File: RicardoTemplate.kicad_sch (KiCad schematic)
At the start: 38 parts, among them J1 RBUS, U1 ESP32-S3, Y1 R940000171

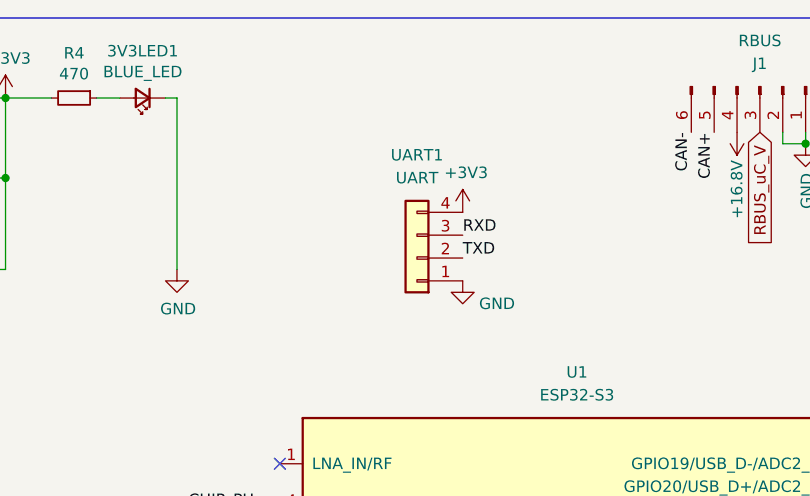
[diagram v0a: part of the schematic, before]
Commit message: Changed UART connector
Now with 1000% more nanofit!
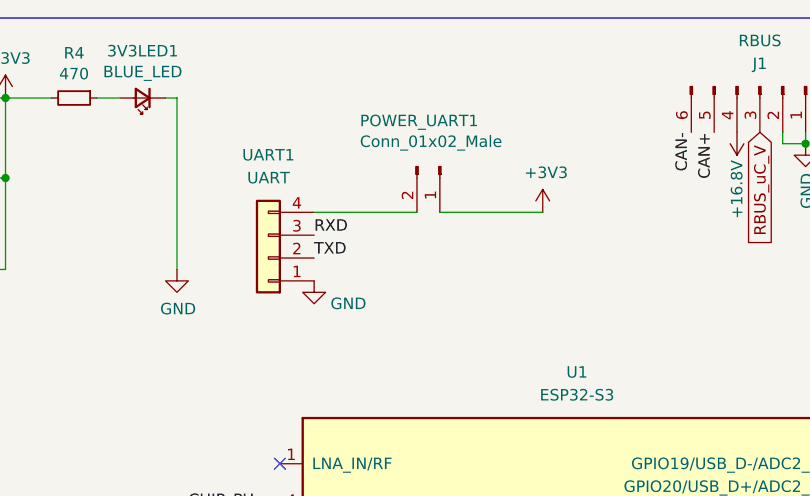
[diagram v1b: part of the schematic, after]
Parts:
- added POWER_UART1: Conn_01x02_Male, Connector_PinHeader_2.54mm:PinHeader_1x02_P2.54mm_Vertical, symbol Connector:Conn_01x02_Male
- UART1: footprint Connector_Molex:Molex_Mini-Fit_Jr_5566-04A_2x02_P4.20mm_Vertical -> Connector_Molex:Molex_Nano-Fit_105309-xx04_1x04_P2.50mm_Vertical
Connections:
- net +3V3: now also POWER_UART1.1 (Pin_1); no longer UART1.4 (Pin_4)
- new net: POWER_UART1.2 (Pin_2), UART1.4 (Pin_4)
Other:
- moved on the sheet: UART1
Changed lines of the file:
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@@
 	(wire
 		(pts
+			(xy 85.09 34.29) (xy 73.66 34.29)
+		)
+		(stroke
+			(width 0)
+			(type default)
+		)
+	)
+	(wire
+		(pts
 			(xy 156.21 127) (xy 156.21 128.27)
 		)
@@
 	(wire
 		(pts
+			(xy 99.06 34.29) (xy 87.63 34.29)
+		)
+		(stroke
+			(width 0)
+			(type default)
+		)
+	)
+	(wire
+		(pts
 			(xy 27.94 30.48) (xy 30.48 30.48)
 		)
@@
 	)
 	(label "RXD"
-		(at 90.17 36.83 0)
+		(at 73.66 36.83 0)
 		(fields_autoplaced yes)
 		(effects
@@
 	)
 	(label "TXD"
-		(at 90.17 39.37 0)
+		(at 73.66 39.37 0)
 		(fields_autoplaced yes)
 		(effects
@@
 	(symbol
 		(lib_id "power:+3.3V")
-		(at 90.17 34.29 0)
+		(at 99.06 34.29 0)
 		(unit 1)
 		(exclude_from_sim no)
@@
 		(dnp no)
 		(property "Reference" "#PWR052"
-			(at 90.17 38.1 0)
+			(at 99.06 38.1 0)
 			(effects
 				(font
@@
 		)
 		(property "Value" "+3V3"
-			(at 90.551 29.8958 0)
+			(at 99.441 29.8958 0)
 			(effects
 				(font
@@
 		)
 		(property "Footprint" ""
-			(at 90.17 34.29 0)
+			(at 99.06 34.29 0)
 			(effects
 				(font
@@
 		)
 		(property "Datasheet" ""
-			(at 90.17 34.29 0)
+			(at 99.06 34.29 0)
 			(effects
 				(font
@@
 		)
 		(property "Description" ""
-			(at 90.17 34.29 0)
+			(at 99.06 34.29 0)
 			(effects
 				(font
@@
 	(symbol
 		(lib_id "Connector_Generic:Conn_01x04")
-		(at 85.09 39.37 180)
+		(at 68.58 39.37 180)
 		(unit 1)
 		(exclude_from_sim no)
@@
 		(fields_autoplaced yes)
 		(property "Reference" "UART1"
-			(at 85.09 27.94 0)
+			(at 68.58 27.94 0)
 			(effects
 				(font
@@
 		)
 		(property "Value" "UART"
-			(at 85.09 30.48 0)
+			(at 68.58 30.48 0)
 			(effects
 				(font
@@
 			)
 		)
-		(property "Footprint" "Connector_Molex:Molex_Mini-Fit_Jr_5566-04A_2x02_P4.20mm_Vertical"
-			(at 85.09 39.37 0)
+		(property "Footprint" "Connector_Molex:Molex_Nano-Fit_105309-xx04_1x04_P2.50mm_Vertical"
+			(at 68.58 39.37 0)
 			(effects
 				(font
@@
 		)
 		(property "Datasheet" "~"
-			(at 85.09 39.37 0)
+			(at 68.58 39.37 0)
 			(effects
 				(font
@@
 		)
 		(property "Description" "Generic connector, single row, 01x04, script generated (kicad-library-utils/schlib/autogen/connector/)"
-			(at 85.09 39.37 0)
+			(at 68.58 39.37 0)
 			(effects
 				(font
@@
 	(symbol
 		(lib_id "power:GND")
-		(at 90.17 41.91 0)
+		(at 73.66 41.91 0)
 		(unit 1)
 		(exclude_from_sim no)
@@
 		(dnp no)
 		(property "Reference" "#PWR053"
-			(at 90.17 48.26 0)
+			(at 73.66 48.26 0)
 			(effects
 				(font
@@
 		)
 		(property "Value" "GND"
-			(at 93.98 44.45 0)
+			(at 77.47 44.45 0)
 			(effects
 				(font
@@
 		)
 		(property "Footprint" ""
-			(at 90.17 41.91 0)
+			(at 73.66 41.91 0)
 			(effects
 				(font
@@
 		)
 		(property "Datasheet" ""
-			(at 90.17 41.91 0)
+			(at 73.66 41.91 0)
 			(effects
 				(font
@@
 		)
 		(property "Description" ""
-			(at 90.17 41.91 0)
+			(at 73.66 41.91 0)
 			(effects
 				(font
@@
 					(unit 1)
 				)
+			)
+		)
+	)
+	(symbol
+		(lib_id "Connector:Conn_01x02_Male")
+		(at 87.63 29.21 270)
+		(unit 1)
+		(exclude_from_sim no)
+		(in_bom yes)
+		(on_board yes)
+		(dnp no)
+		(property "Reference" "POWER_UART1"
+			(at 78.74 24.13 90)
+			(effects
+				(font
+					(size 1.27 1.27)
+				)
+				(justify left)
+			)
+		)
+		(property "Value" "Conn_01x02_Male"
+			(at 78.74 26.4414 90)
+			(effects
+				(font
+					(size 1.27 1.27)
+				)
+				(justify left)
+			)
+		)
+		(property "Footprint" "Connector_PinHeader_2.54mm:PinHeader_1x02_P2.54mm_Vertical"
+			(at 87.63 29.21 0)
+			(effects
+				(font
+					(size 1.27 1.27)
+				)
+				(hide yes)
+			)
+		)
+		(property "Datasheet" "~"
+			(at 87.63 29.21 0)
+			(effects
+				(font
+					(size 1.27 1.27)
+				)
+				(hide yes)
+			)
+		)
+		(property "Description" ""
+			(at 87.63 29.21 0)
+			(effects
+				(font
+					(size 1.27 1.27)
+				)
+				(hide yes)
+			)
+		)
+		(pin "1"
+		)
+		(pin "2"
+		)
+		(instances
+			(project "RicardoTemplate"
+				(path "/7db990e4-92e1-4f99-b4d2-435bbec1ba83"
+					(reference "POWER_UART1")
+					(unit 1)
+				)

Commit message: Changed uart conn
Get transposed!
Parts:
- UART1: footprint Connector_Molex:Molex_Nano-Fit_105309-xx04_1x04_P2.50mm_Vertical -> Connector_Molex:Molex_Nano-Fit_105313-xx03_1x03_P2.50mm_Horizontal
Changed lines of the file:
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@@
 			)
 		)
-		(property "Footprint" "Connector_Molex:Molex_Nano-Fit_105309-xx04_1x04_P2.50mm_Vertical"
+		(property "Footprint" "Connector_Molex:Molex_Nano-Fit_105313-xx03_1x03_P2.50mm_Horizontal"
 			(at 68.58 39.37 0)
 			(effects

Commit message: Minor improvements
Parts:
- added R25, R26, R29, R30: 20-100, Resistor_SMD:R_0402_1005Metric, symbol Device:R_Small
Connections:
- net CS: now also R25.1; no longer U1.32 (SPICS0/GPIO29)
- net MISO: now also R30.1; no longer U1.35 (SPID/GPIO32)
- net MOSI: now also R29.1; no longer U1.34 (SPIQ/GPIO31)
- net SCK: now also R26.1; no longer U1.33 (SPICLK/GPIO30)
- new net: R29.2, U1.34 (SPIQ/GPIO31)
- new net: R25.2, U1.32 (SPICS0/GPIO29)
- new net: R26.2, U1.33 (SPICLK/GPIO30)
- new net: R30.2, U1.35 (SPID/GPIO32)
